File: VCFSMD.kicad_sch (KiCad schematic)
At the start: 89 parts, among them J1 Conn_01x06_Pin, J10 AudioJack2, J11 AudioJack2, J12 AudioJack2, J13 AudioJack2, J14 Conn_01x06_Pin, J2 Conn_02x05_Odd_Even, J3 Conn_01x07_Pin, J4 Conn_01x07_Pin, J5 AudioJack2, J6 AudioJack2, J7 AudioJack2, J8 AudioJack2, J9 AudioJack2, Q1 BC857, Q2 BC857, Q3 BC847, SW1 SW_SPDT, U1 TL074, U2 L7809, U3 TL074, U4 TL074, U5 LM13700, U6 LM7909

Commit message: Add files via upload
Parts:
- removed C6, C8: 1u, Capacitor_SMD:C_1206_3216Metric, symbol Device:C
- removed J1, J14: Conn_01x06_Pin, Connector_PinHeader_2.54mm:PinHeader_1x06_P2.54mm_Vertical, symbol Connector:Conn_01x06_Pin
- removed J3, J4: Conn_01x07_Pin, Connector_PinHeader_2.54mm:PinHeader_1x07_P2.54mm_Vertical, symbol Connector:Conn_01x07_Pin
- removed U2: L7809, Package_TO_SOT_SMD:SOT-223, symbol Regulator_Linear:L7809
- removed U6: LM7909, Package_TO_SOT_SMD:SOT-223, symbol Regulator_Linear:LM7909_TO220
- added C101, C102, C103, C104: 10u, Capacitor_SMD:C_1206_3216Metric, symbol Device:C
- added J101, J104: Conn_01x08_Pin, Connector_PinSocket_2.54mm:PinSocket_1x08_P2.54mm_Vertical, symbol Connector:Conn_01x08_Pin
- added J102, J103: Conn_01x09_Pin, Connector_PinHeader_2.54mm:PinHeader_1x09_P2.54mm_Vertical, symbol Connector:Conn_01x09_Pin
- added R101, R104: 1k, Resistor_SMD:R_1206_3216Metric, symbol Device:R
- added R102, R103: 6k2, Resistor_SMD:R_1206_3216Metric, symbol Device:R
- added U101: LM317_SOT-223, Package_TO_SOT_SMD:SOT-223-3_TabPin2, symbol Regulator_Linear:LM317_SOT-223
- added U102: LM337_SOT223, Package_TO_SOT_SMD:SOT-223-3_TabPin2, symbol Regulator_Linear:LM337_SOT223
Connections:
- net +12V: now also C102.2, U101.3 (VI)
- net +9V: now also C103.1, J102.5 (Pin_5), J103.5 (Pin_5), R101.1, U101.2 (VO)
- net -12V: now also C101.1, U102.2 (VI)
- net -9V: now also C104.1, J102.6 (Pin_6), J103.6 (Pin_6), R104.2, U102.3 (VO)
- net AUDSUM: now also J101.2 (Pin_2), J104.2 (Pin_2)
- net BP: now also J102.2 (Pin_2), J103.2 (Pin_2)
- net BP_INV: now also J101.7 (Pin_7), J104.7 (Pin_7)
- net BP_POT: now also J102.1 (Pin_1), J103.1 (Pin_1)
- net GND: now also D11.1 (K), C101.2, C102.1, C103.2, C104.2, J102.7 (Pin_7), J103.7 (Pin_7), R102.2, R103.1; no longer R12.1
- net LED: now also J101.6 (Pin_6), J104.6 (Pin_6)
- net OUT_BP: now also J102.9 (Pin_9), J103.9 (Pin_9)
- net OUT_BS: now also J101.5 (Pin_5), J104.5 (Pin_5)
- net OUT_HP: now also J101.8 (Pin_8), J104.8 (Pin_8)
- net OUT_LP: now also J102.8 (Pin_8), J103.8 (Pin_8)
- net VGNDCV: now also J102.3 (Pin_3), J103.3 (Pin_3)
- net PINGIN: now reaches J9.T, R42.1
- net PINGIN: now also C7.2, J101.4 (Pin_4), J104.4 (Pin_4); no longer C7.1
- net at R12.2: now also Q3.2 (E); no longer D11.1 (K)
- net SW12: now reaches R4.1, SW1.2 (B)
- net SW12: now also J101.3 (Pin_3), J104.3 (Pin_3)
- net at D2.2 (A), R31.1: now also C7.1; no longer C7.2
- net PINGLED: now reaches D11.2 (A)
- net PINGLED: now also R12.1, J101.1 (Pin_1), J104.1 (Pin_1); no longer Q3.2 (E)
- new net: R101.2, R102.1, U101.1 (ADJ)
- new net: R103.2, R104.1, U102.1 (ADJ)
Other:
- title: VCF2 by github.com/Fihdi -> SVF12 by github.com/Fihdi
- moved on the sheet: C7, D11, J9, R1, R12, R39

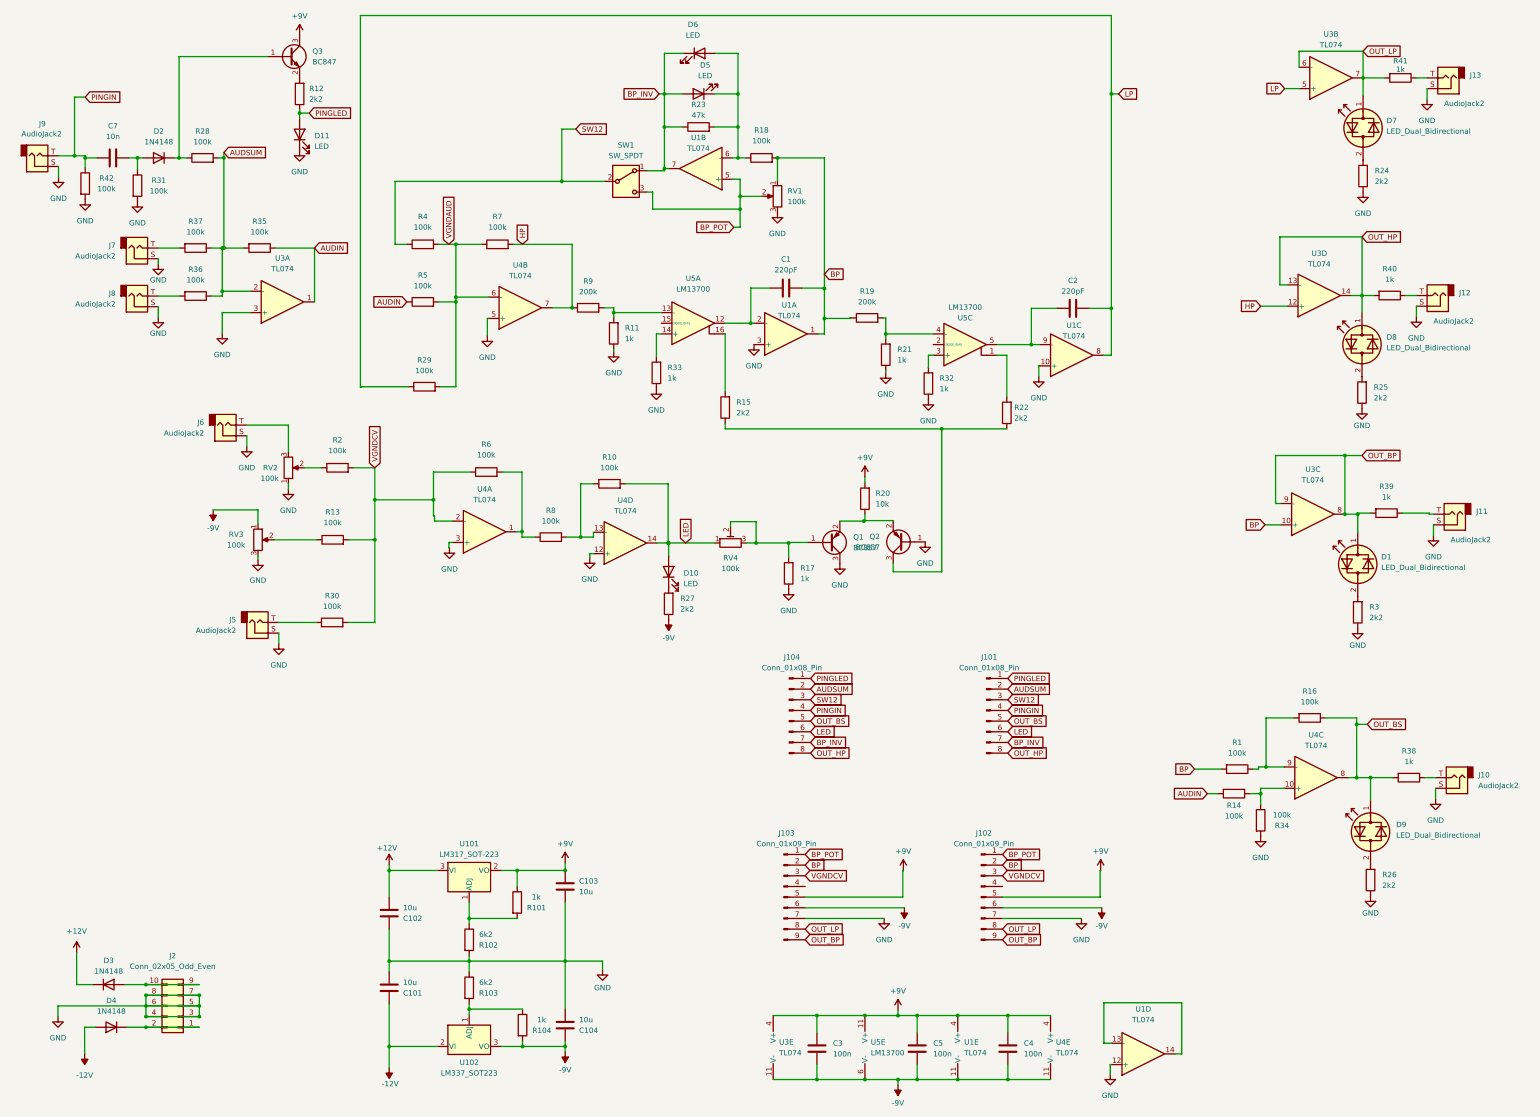
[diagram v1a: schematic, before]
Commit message: Changed mounting holes for spacers from M2 to M2.5
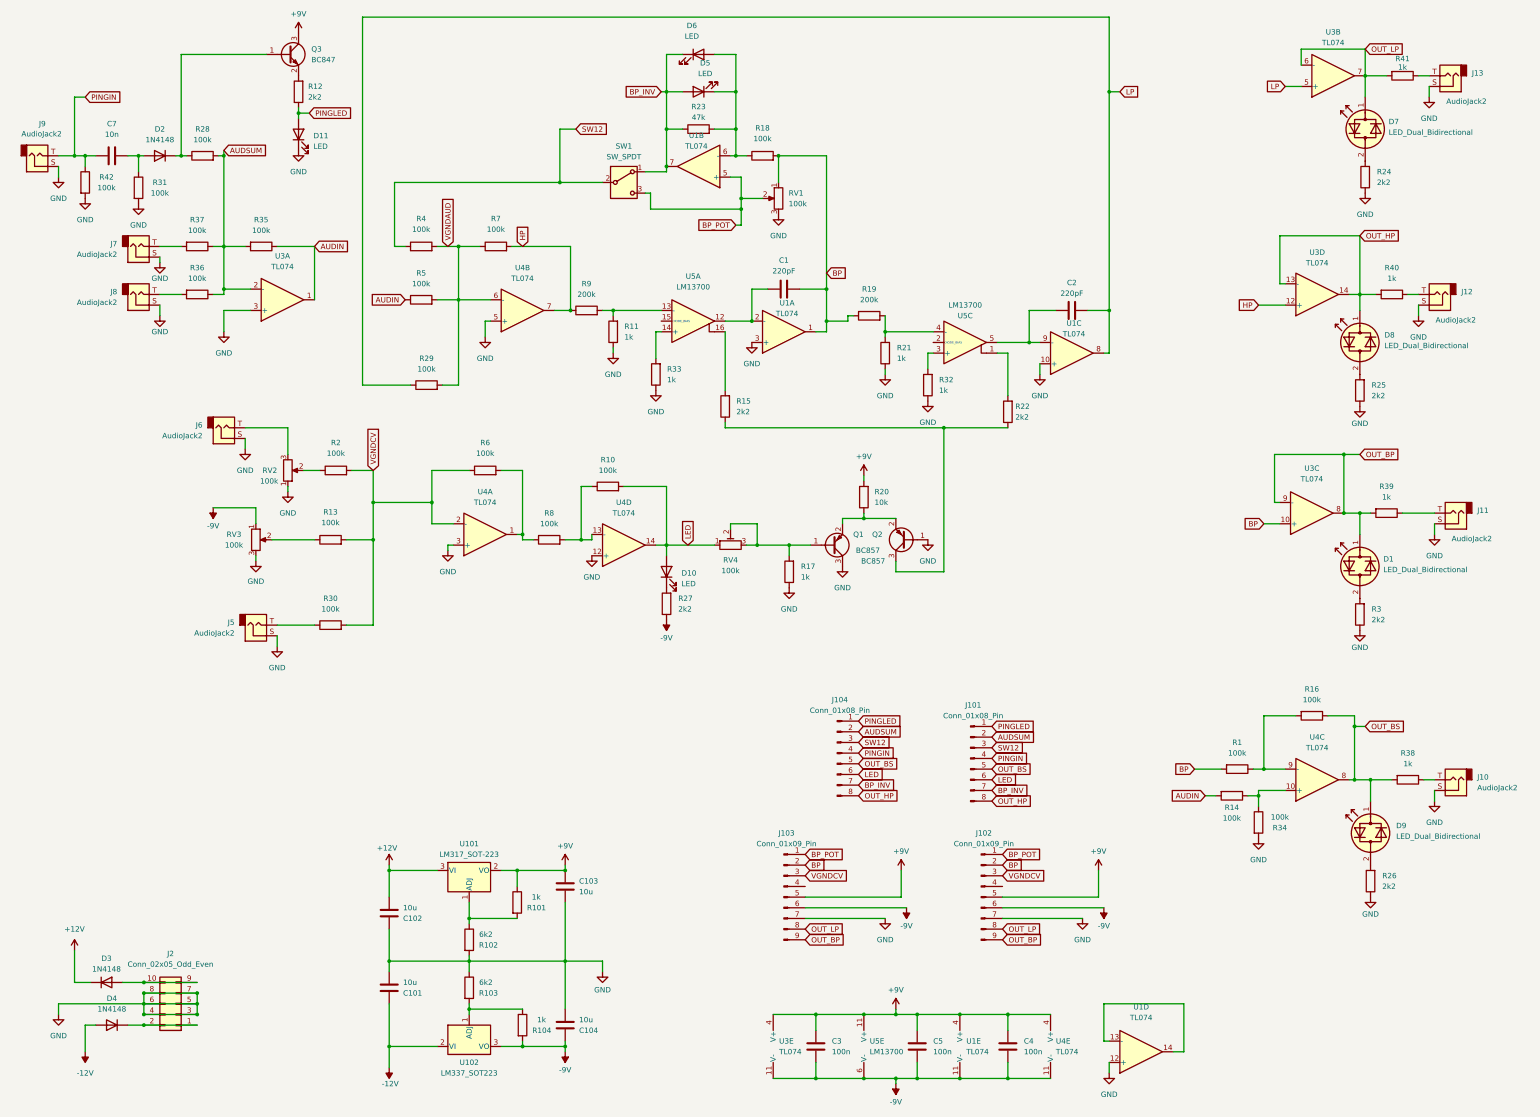
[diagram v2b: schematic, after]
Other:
- moved on the sheet: C1, C2, C3, C4, C5, C7, D1, D10, D2, D3, D4, D5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

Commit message: Add files via upload
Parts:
- removed J101: Conn_01x08_Pin, Connector_PinSocket_2.54mm:PinSocket_1x08_P2.54mm_Vertical, symbol Connector:Conn_01x08_Pin
- removed J102: Conn_01x09_Pin, Connector_PinHeader_2.54mm:PinHeader_1x09_P2.54mm_Vertical, symbol Connector:Conn_01x09_Pin
- added J101: Conn_01x09_Pin, Connector_PinHeader_2.54mm:PinHeader_1x09_P2.54mm_Vertical, symbol Connector:Conn_01x09_Pin
- added J102: Conn_01x08_Pin, Connector_PinSocket_2.54mm:PinSocket_1x08_P2.54mm_Vertical, symbol Connector:Conn_01x08_Pin
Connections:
- net +9V: now also J101.5 (Pin_5)
- net -9V: now also J101.6 (Pin_6)
- net AUDIN: now also U1.14; no longer U3.1
- net AUDSUM: now also U1.13 (-), J102.2 (Pin_2); no longer U3.2 (-)
- net BP: now also R3.1, R39.2, J101.2 (Pin_2); no longer U3.10 (+)
- net BP_INV: now also J102.7 (Pin_7)
- net BP_POT: now also J101.1 (Pin_1)
- net GND: now also U3.10 (+), U3.12 (+), U3.5 (+), J101.7 (Pin_7); no longer R24.1, R25.1, R3.1
- net HP: now also J104.8 (Pin_8), R25.1, R40.2, J102.8 (Pin_8); no longer U3.12 (+)
- net LED: now also J102.6 (Pin_6)
- net LP: now also J103.8 (Pin_8), R24.1, R41.2, J101.8 (Pin_8); no longer U3.5 (+)
- net OUT_BS: now also J102.5 (Pin_5)
- net PINGIN: now also J102.4 (Pin_4)
- net PINGLED: now also J102.1 (Pin_1)
- net SW12: now also J102.3 (Pin_3)
- net VGNDCV: now also J101.3 (Pin_3)
- net at D1.2 (AK), R3.2: now also U3.9 (-)
- net at D7.2 (AK), R24.2: now also U3.6 (-)
- net at D8.2 (AK), R25.2: now also U3.13 (-)
- removed net OUT_BP: D1.1 (KA), J103.9 (Pin_9), R39.2, U3.8, U3.9 (-)
- removed net OUT_HP: D8.1 (KA), J104.8 (Pin_8), R40.2, U3.13 (-), U3.14
- removed net OUT_LP: D7.1 (KA), J103.8 (Pin_8), R41.2, U3.6 (-), U3.7
- new net: U3.1, U3.2 (-)
- new net: D8.1 (KA), U3.14
- new net: D7.1 (KA), U3.7
- new net: D1.1 (KA), U3.8
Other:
- moved on the sheet: C1, C2, D1, D6, D7, D8, J13, R19, R23, R24, R25, R3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
